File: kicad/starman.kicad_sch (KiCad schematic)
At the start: 237 parts, among them J1 M20-8771246, J10 PJ-063AH, J11 Conn_02x01, J2 M20-8771246, J3 M20-8771246, J4 ESW-106-44-T-S, J5 PH2-06-UA, J6 ESW-112-44-T-S, J7 Conn_01x10, J8 ESW-112-44-T-S, J9 Conn_01x10, SW1 PTS810 SJM 250 SMTR LFS, SW2 PTS810 SJM 250 SMTR LFS, SW3 SW_SPST, U1 ESP32-S2-MINI-1, U10 LED1642GWTTR, U11 AZ1084CS2-ADJ, U12 BA33BC0FP-E2, U13 IS31AP4991-SLS2, U2 LED1642GWTTR, U3 LED1642GWTTR, U4 LED1642GWTTR, U5 LED1642GWTTR, U6 LED1642GWTTR, U7 LED1642GWTTR, U8 LED1642GWTTR, U9 LED1642GWTTR, X1 ECS-2333-300, X2 ECS-2333-300, X3 ECS-2333-300

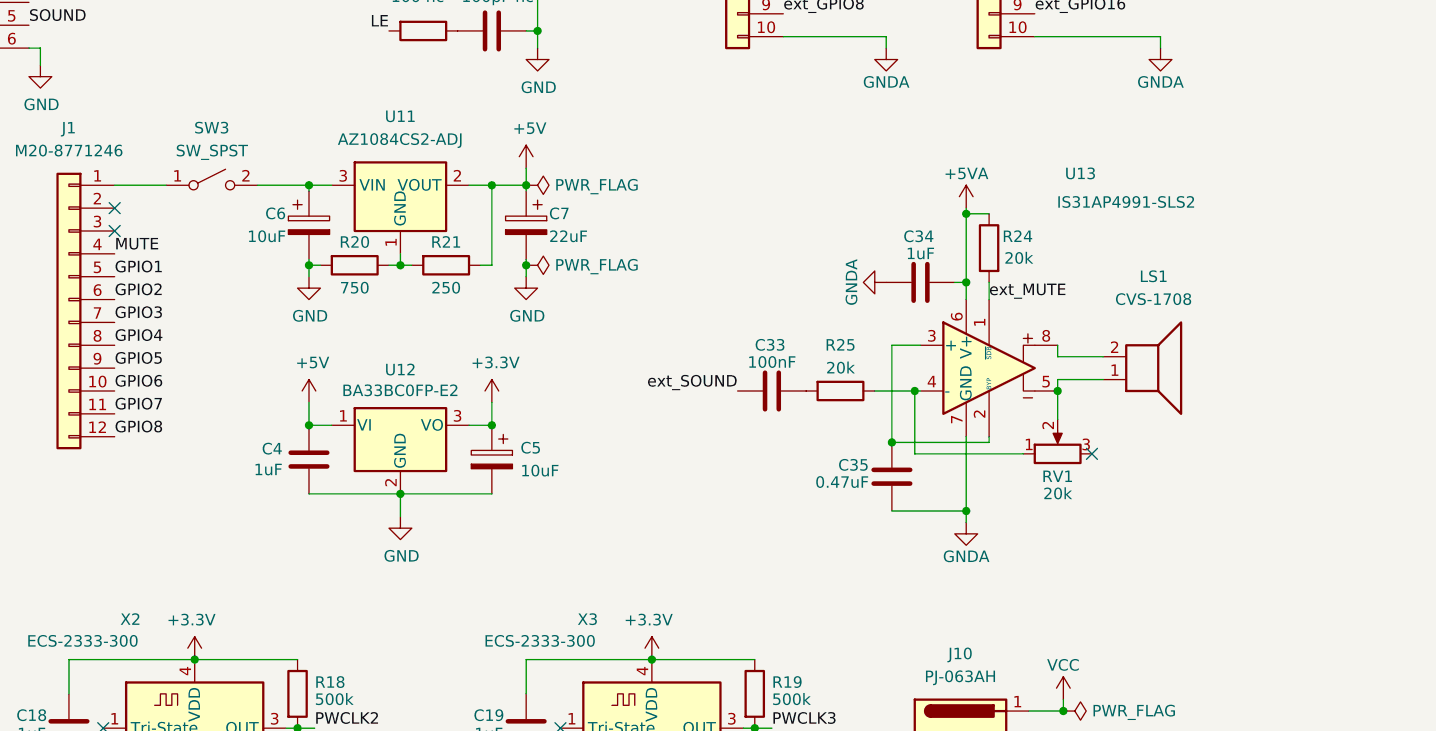
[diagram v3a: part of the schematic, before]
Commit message: Upgrade from IS31AP4991-SLS2 to PAM8302AAS
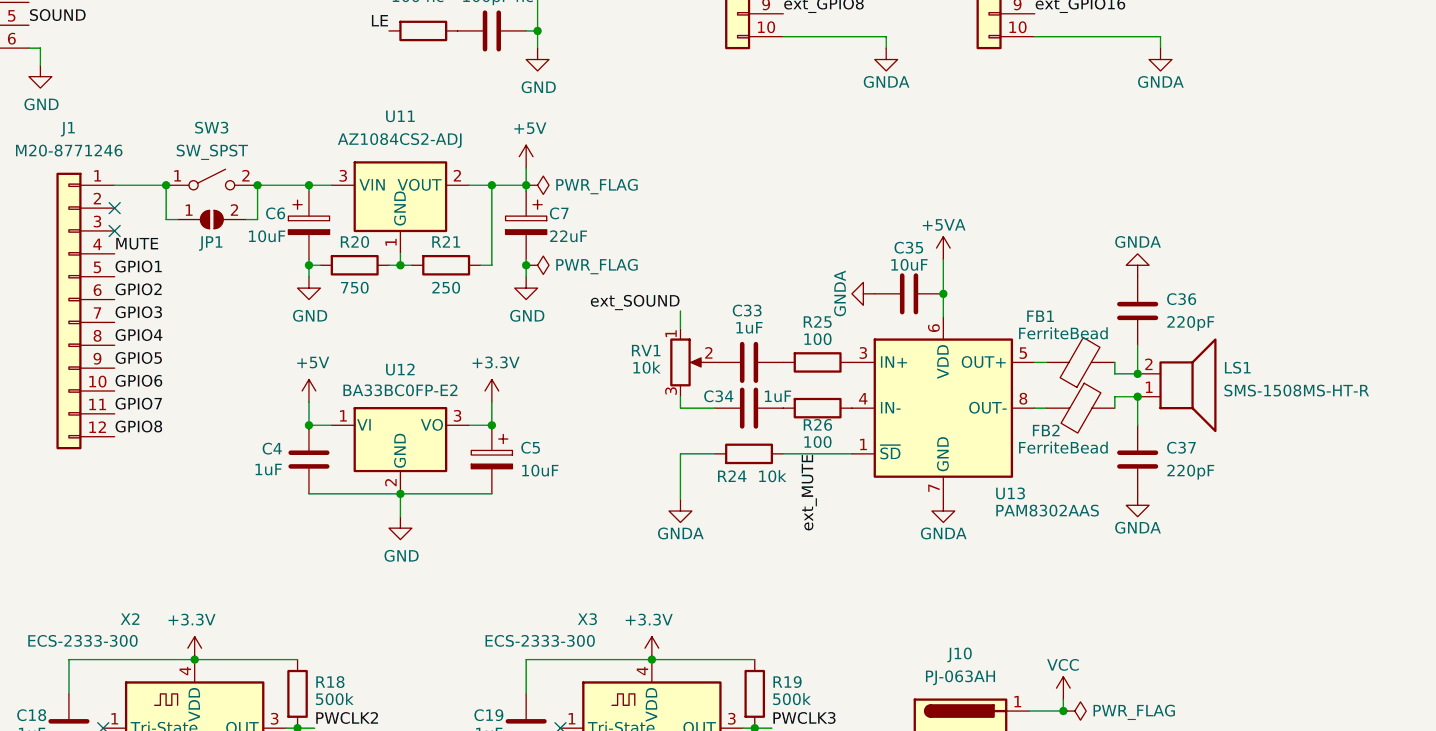
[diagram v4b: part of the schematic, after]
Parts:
- removed U13: IS31AP4991-SLS2, Package_SO:MSOP-8_3x3mm_P0.65mm, symbol Amplifier_Audio:IS31AP4991-SLS2
- added C36, C37: 220pF, Capacitor_SMD:C_0805_2012Metric, symbol Device:C
- added FB1, FB2: FerriteBead, Capacitor_SMD:C_0805_2012Metric, symbol Device:FerriteBead
- added JP1: SolderJumper_2_Open, Jumper:SolderJumper-2_P1.3mm_Open_RoundedPad1.0x1.5mm, symbol Jumper:SolderJumper_2_Open
- added R26: 100, Resistor_SMD:R_0805_2012Metric, symbol Device:R
- added U13: PAM8302AAS, Package_SO:SOP-8_3.9x4.9mm_P1.27mm, symbol Amplifier_Audio:PAM8302AAS
- C33: value 100nF -> 1uF
- C35: value 0.47uF -> 10uF
- LS1: value CVS-1708 -> SMS-1508MS-HT-R; footprint Buzzer_Beeper:MagneticBuzzer_StarMicronics_HMB-06_HMB-12 -> starman:SMS-1508MS-HT-R
- R24, RV1: value 20k -> 10k
- R25: value 20k -> 100
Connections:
- net +5VA: now also C35.1, U13.6 (VDD); no longer C34.1, R24.1
- net GNDA: now also R24.2, C36.1, C37.2, U13.7 (GND); no longer C34.2
- net ext_MUTE: now also R24.1, U13.1 (~{SD}); no longer R24.2
- net ext_SOUND: now also RV1.1; no longer C33.2
- net at J1.1 (Pin_1), SW3.1 (A): now also JP1.1 (A)
- net at C6.1, SW3.2 (B), U11.3 (VIN): now also JP1.2 (B)
- net at RV1.2: now also C33.2; no longer LS1.1
- net at LS1.2: now also C36.2, FB1.2
- net at R25.1: now also U13.3 (IN+); no longer RV1.1
- net at RV1.3: now also C34.2
- new net: R26.1, U13.4 (IN-)
- new net: FB1.1, U13.5 (OUT+)
- new net: FB2.2, U13.8 (OUT-)
- new net: C37.1, FB2.1, LS1.1
- new net: C34.1, R26.2
- no-connect marks 18 -> 17
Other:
- moved on the sheet: LS1, RV1

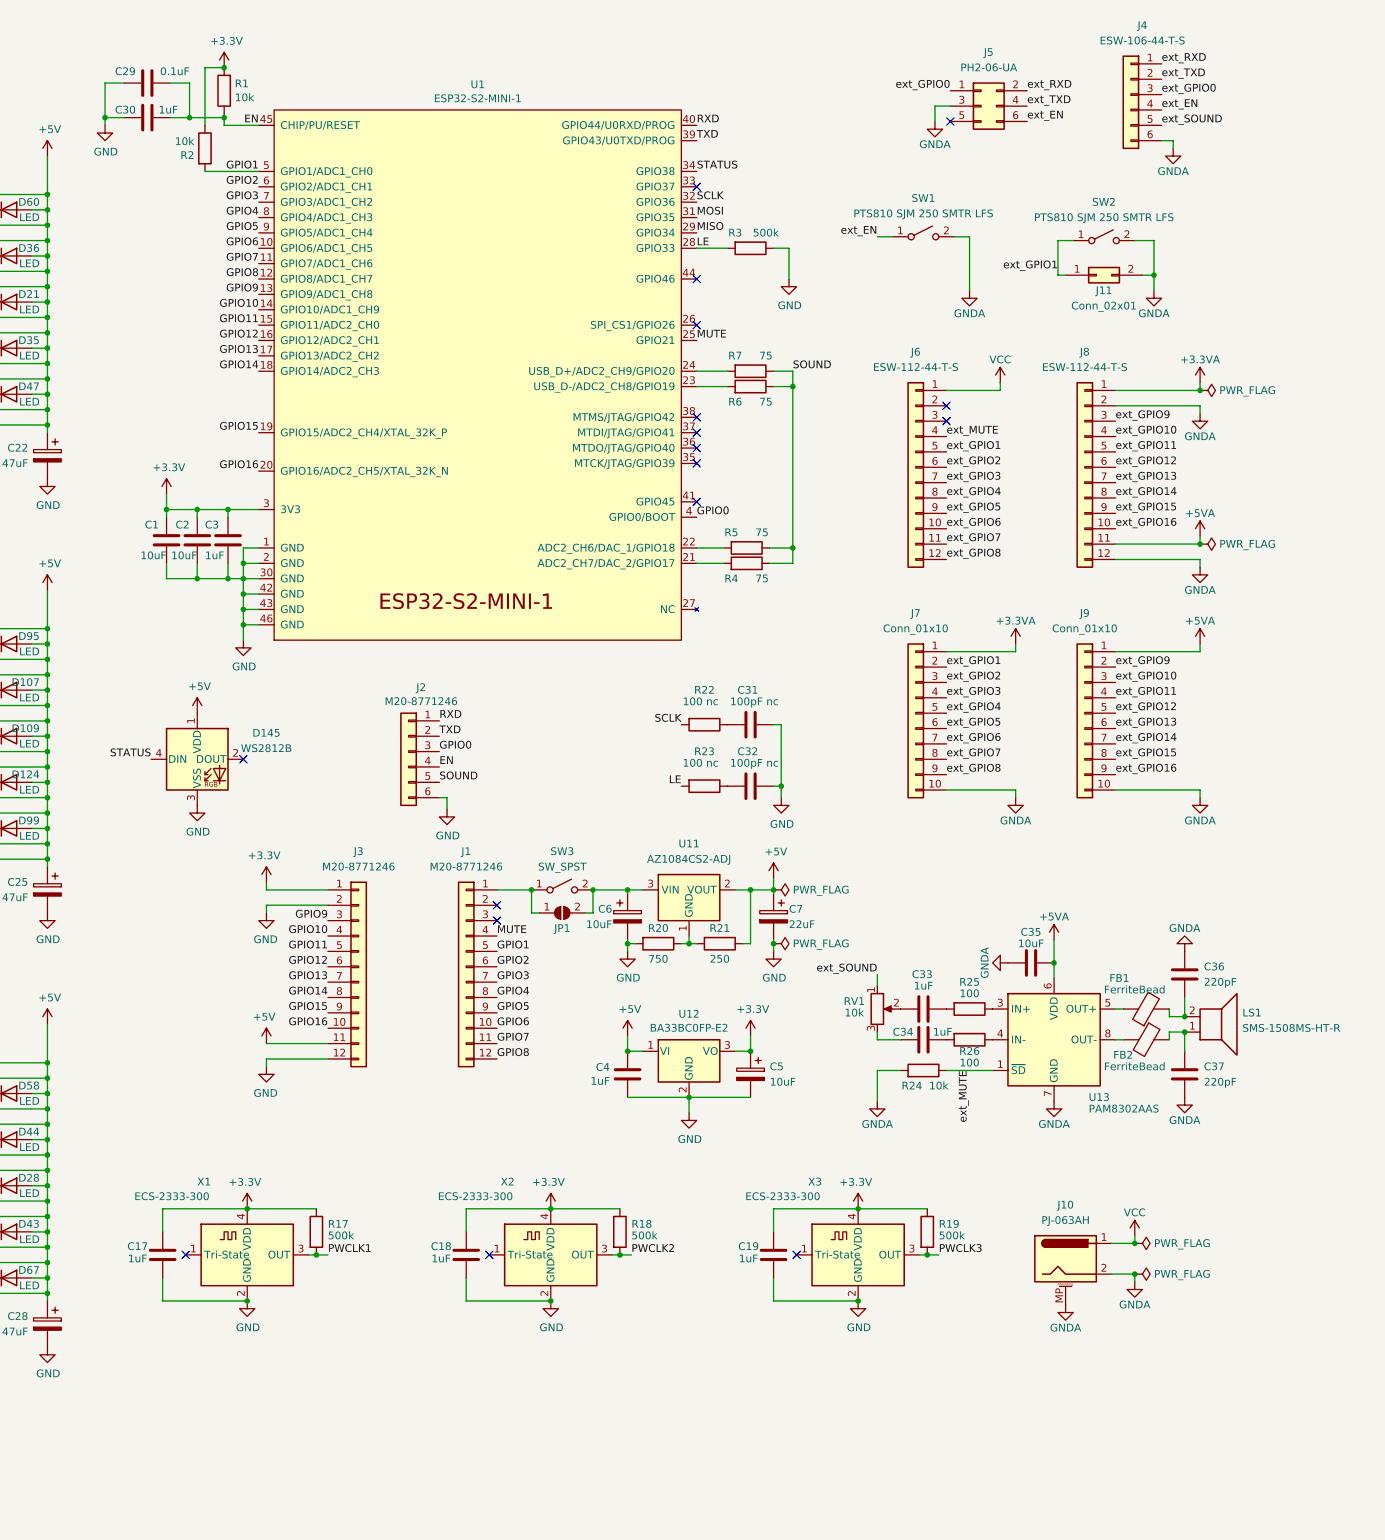
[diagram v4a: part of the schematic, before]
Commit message: Added band-pass filter into PCB
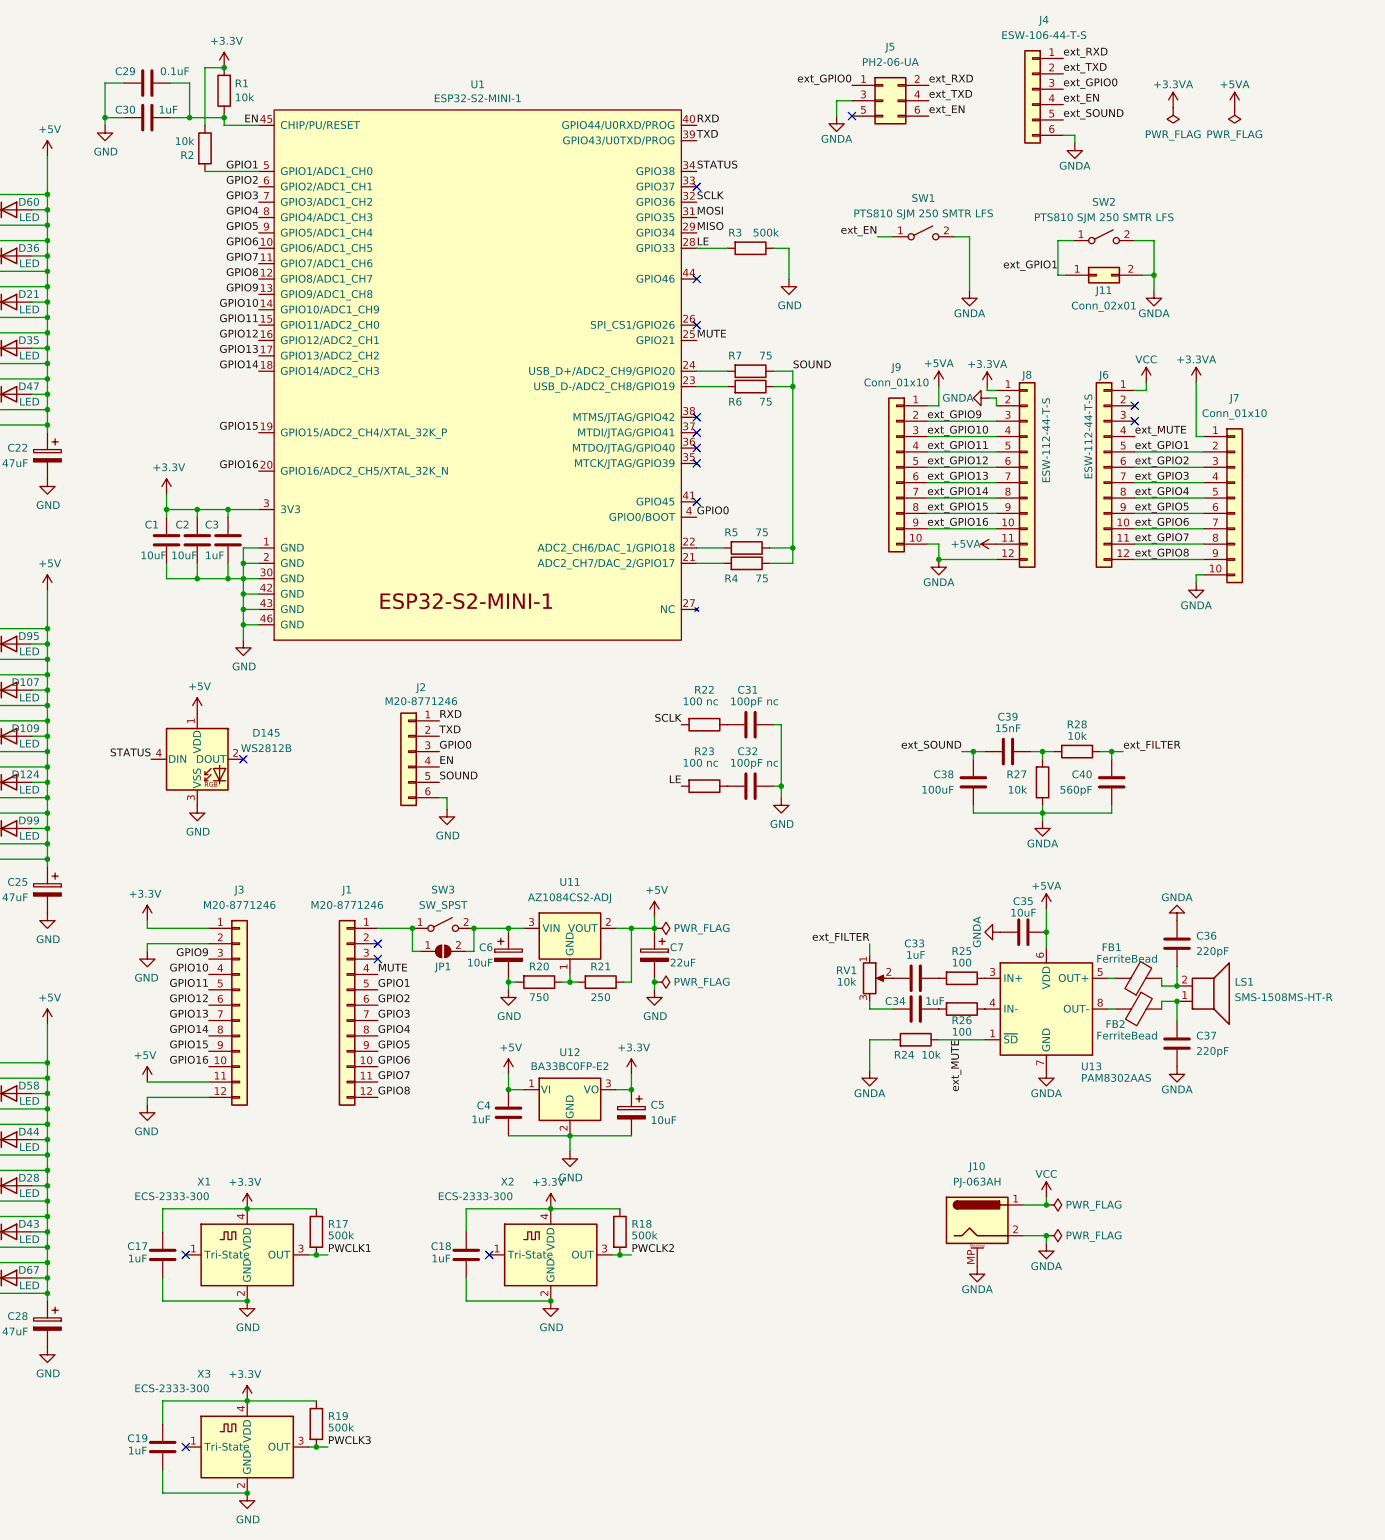
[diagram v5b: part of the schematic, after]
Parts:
- added C38: 100uF, Capacitor_SMD:C_0805_2012Metric, symbol Device:C
- added C39: 15nF, Capacitor_SMD:C_0805_2012Metric, symbol Device:C
- added C40: 560pF, Capacitor_SMD:C_0805_2012Metric, symbol Device:C
- added R27, R28: 10k, Resistor_SMD:R_0805_2012Metric, symbol Device:R
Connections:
- net GNDA: now also C38.2, C40.2, R27.1
- net ext_SOUND: now also C38.1, C39.2; no longer RV1.1
- new net: C39.1, R27.2, R28.2
- new net ext_FILTER: C40.1, R28.1, RV1.1
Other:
- moved on the sheet: C19, C33, C34, C35, C36, C37, C4, C5, C6, C7, FB1, FB2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

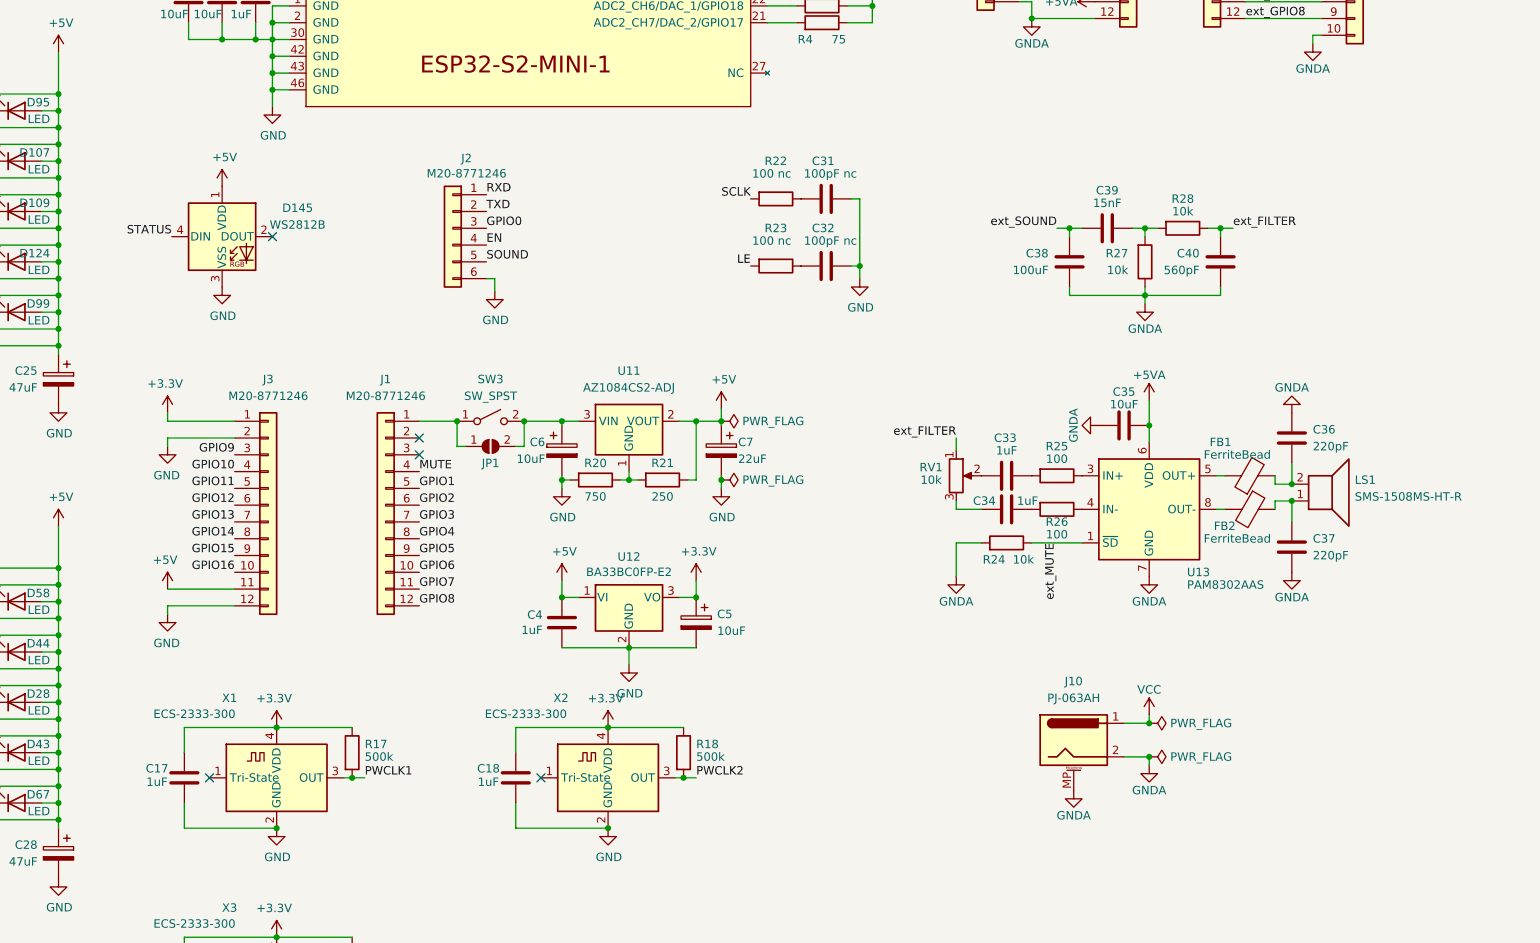
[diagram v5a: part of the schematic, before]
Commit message: Scrap the band-pass filter; get the proper 3d model for the speaker candidate
Tests showed it wasn't necessary
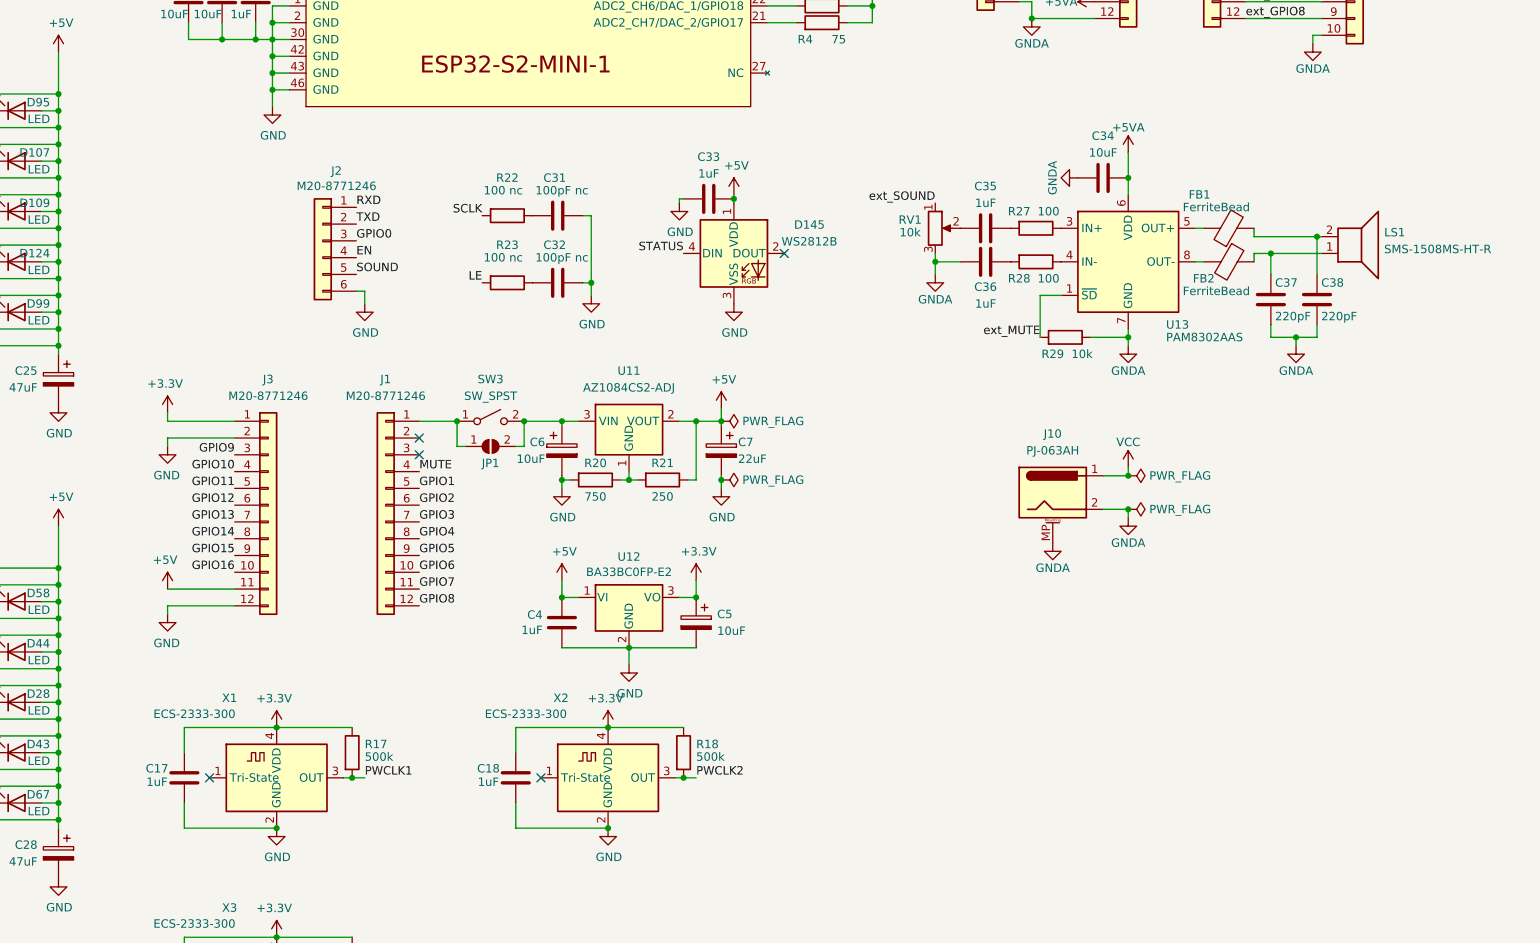
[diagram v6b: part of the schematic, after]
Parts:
- removed C38: 100uF, Capacitor_SMD:C_0805_2012Metric, symbol Device:C
- removed C39: 15nF, Capacitor_SMD:C_0805_2012Metric, symbol Device:C
- removed C40: 560pF, Capacitor_SMD:C_0805_2012Metric, symbol Device:C
- removed R27, R28: 10k, Resistor_SMD:R_0805_2012Metric, symbol Device:R
- added C33: 1uF, Capacitor_SMD:C_0805_2012Metric, symbol Device:C
- LS1: footprint starman:SMS-1508MS-HT-R -> starman:SPKR_SMS-1508MS-HT-R
- renumbered C35 to C34, C33 to C35, C34 to C36, C36 to C37, C37 to C38, R25 to R27, R26 to R28, R24 to R29
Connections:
- net ext_FILTER is gone; now on net ext_SOUND: RV1.1
- net +5V: now also C33.1
- net GND: now also C33.2
- net GNDA: now also C36.2, C37.2, R29.1, RV1.3; no longer C37.1, R29.2
- net ext_MUTE: now also R29.2; no longer R29.1
- net at FB2.1, LS1.1: now also C37.1; no longer C38.1
- net at FB1.2, LS1.2: now also C38.1; no longer C37.2
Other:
- moved on the sheet: C31, C32, C34, C35, C36, C37, C38, D145, FB1, FB2, J10, J2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
